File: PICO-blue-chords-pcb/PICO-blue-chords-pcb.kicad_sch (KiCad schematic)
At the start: 27 parts

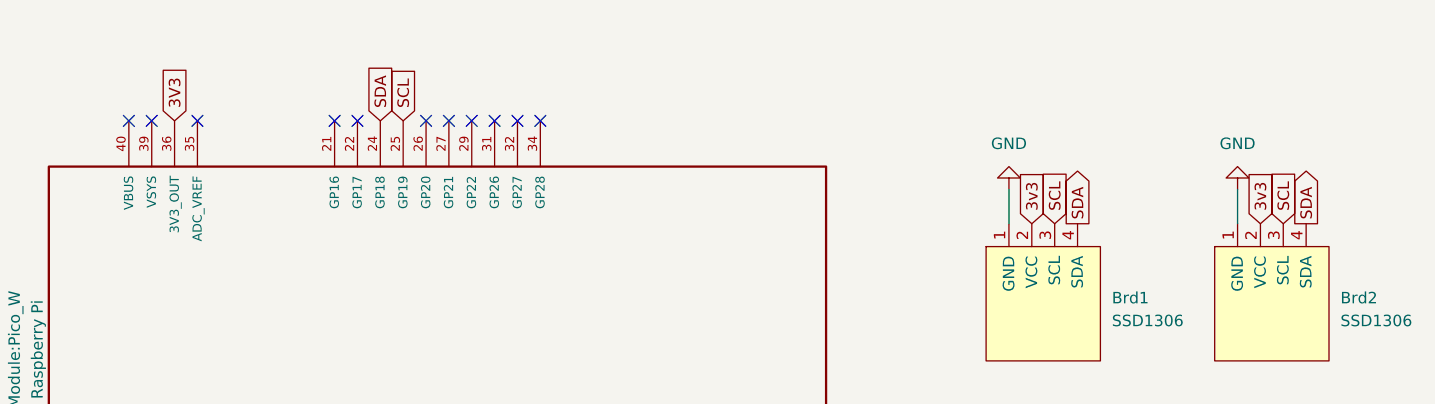
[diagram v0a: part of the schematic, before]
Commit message: Upgraded to use SDK and added missing PCB tracks.
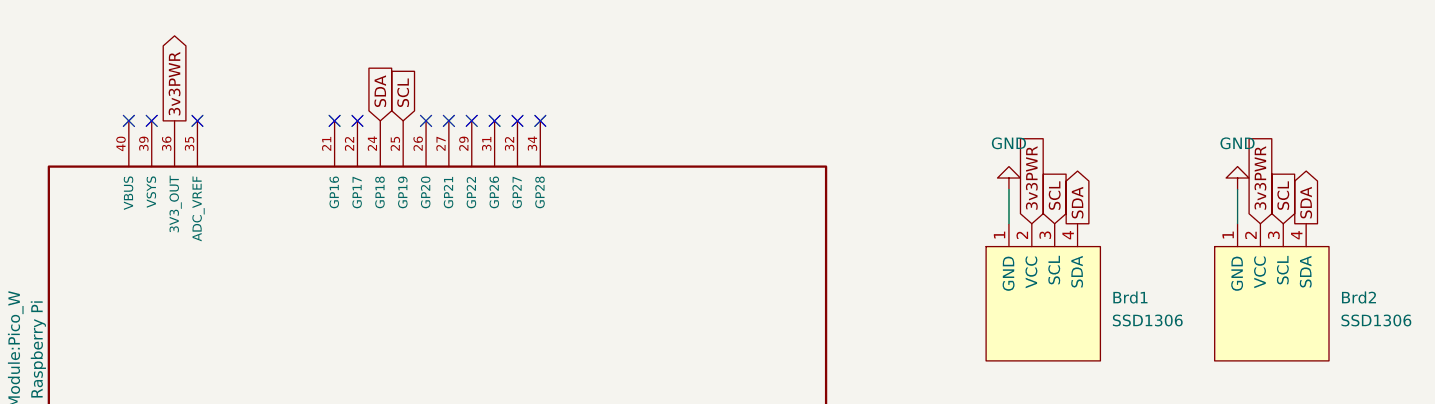
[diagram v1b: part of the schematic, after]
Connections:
- net 3v3 is gone; now on net 3v3PWR: Brd1.2 (VCC), Brd2.2 (VCC)
- net 3V3 renamed 3v3PWR
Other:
- company: (none) -> Rob Miles
- title: (none) -> Blue Chords Keyboard
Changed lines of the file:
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@@
 (kicad_sch (version 20230121) (generator eeschema)
   (paper "A4")
+  (title_block
+    (title "Blue Chords Keyboard")
+    (date "2023-05-23")
+    (rev "2.0")
+    (company "Rob Miles")
+  )
   (junction (at 76.2 162.56) (diameter 0) (color 0 0 0 0)
   )
@@
     )
   )
-  (global_label "3v3" (shape input) (at 185.42 45.72 90) (fields_autoplaced)
-    (effects (font (size 1.27 1.27)) (justify left))
-    (property "Intersheetrefs" "${INTERSHEET_REFS}" (at 185.42 39.4276 90)
+  (global_label "3v3PWR" (shape input) (at 185.42 45.72 90) (fields_autoplaced)
+    (effects (font (size 1.27 1.27)) (justify left))
+    (property "Intersheetrefs" "${INTERSHEET_REFS}" (at 185.42 35.4362 90)
       (effects (font (size 1.27 1.27)) (justify left) hide)
     )
@@
     )
   )
-  (global_label "3v3" (shape input) (at 210.82 45.72 90) (fields_autoplaced)
-    (effects (font (size 1.27 1.27)) (justify left))
-    (property "Intersheetrefs" "${INTERSHEET_REFS}" (at 210.82 39.4276 90)
+  (global_label "3v3PWR" (shape input) (at 210.82 45.72 90) (fields_autoplaced)
+    (effects (font (size 1.27 1.27)) (justify left))
+    (property "Intersheetrefs" "${INTERSHEET_REFS}" (at 210.82 35.4362 90)
       (effects (font (size 1.27 1.27)) (justify left) hide)
     )
@@
     )
   )
-  (global_label "3V3" (shape input) (at 90.17 34.29 90) (fields_autoplaced)
-    (effects (font (size 1.27 1.27)) (justify left))
-    (property "Intersheetrefs" "${INTERSHEET_REFS}" (at 90.17 27.8766 90)
-      (effects (font (size 1.27 1.27)) (justify left) hide)
-    )
+  (global_label "3v3PWR" (shape output) (at 90.17 34.29 90) (fields_autoplaced)
+    (effects (font (size 1.27 1.27)) (justify left))
+    (property "Intersheetrefs" "${INTERSHEET_REFS}" (at 90.17 24.0062 90)
+      (effects (font (size 1.27 1.27)) (justify left) hide)
+    )
